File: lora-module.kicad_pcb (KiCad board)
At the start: 4 copper layers, 20.3 x 22.5 mm, 54 parts, among them J101 Conn_Coaxial, J102 Conn_ARM_SWD_TagConnect_TC203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, Q101 PMN48XP, U201 STM32WLE5CCUx, U301 BALFHB-WL-05D3, U302 BGS12SN6E6327XTSA1, U401 SST26VF080A

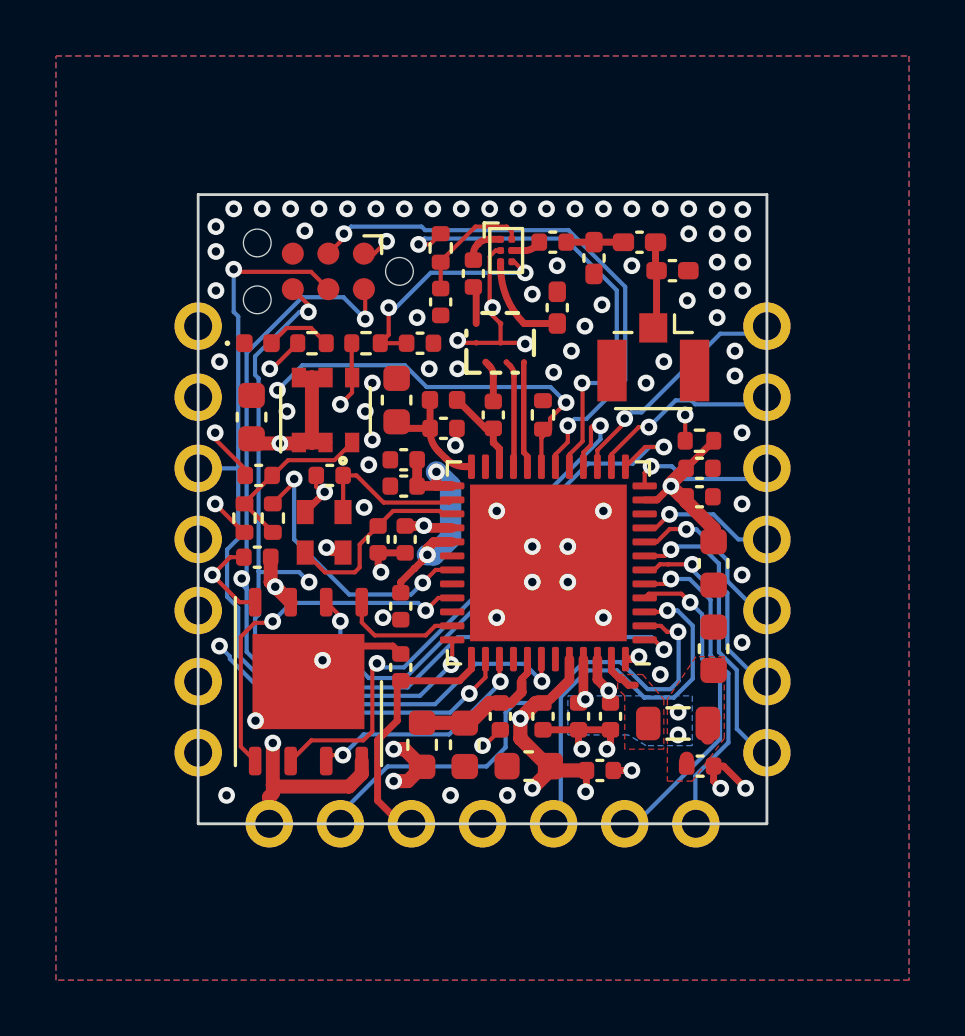
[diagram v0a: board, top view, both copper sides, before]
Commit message: changed XO to TCXO
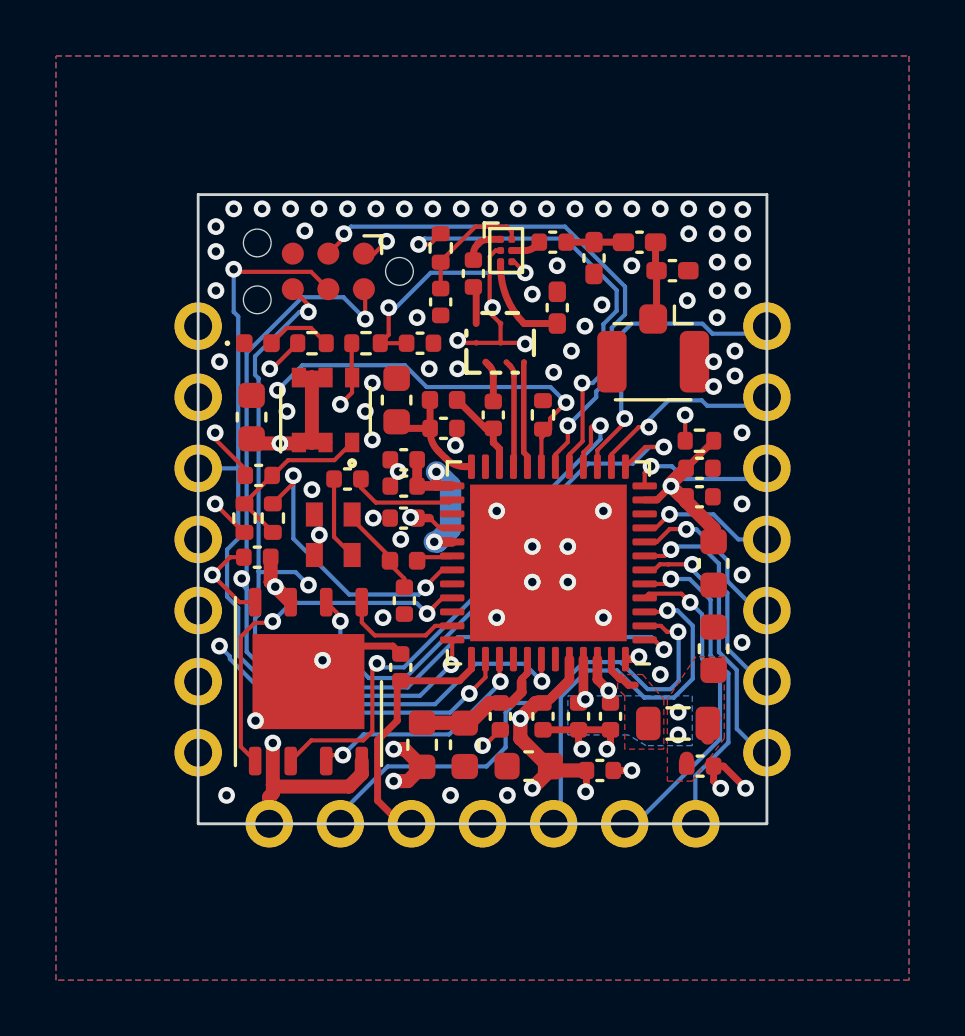
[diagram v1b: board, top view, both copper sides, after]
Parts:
- removed C213: 33p, Capacitor_SMD:C_0402_1005Metric
- removed XTAL201: NX2016SA-32MHZ-EXS00A-CS11336, lora-module:NX2016SA_NDK
- added L203: BLM15HG102SN1D, Inductor_SMD:L_0402_1005Metric, F.Cu at (131.8, 101.9)
- added X201: ECS-TXO-20CSMV4, lora-module:NX2016SA_NDK, F.Cu at (129.3, 100.9)
- C201: value 6.8p -> 33p
- C202: value 6.8 -> 100n
- C217: value 33p -> 100n
- R301, R302: value 100 -> 100R
- moved C202 5.21 mm to (131.8, 103.3), turned to 90 degrees
- moved C201 2.42 mm to (129.8, 98.9), turned to 0 degrees
- moved C209 0.76 mm to (131.8, 100.3), turned to 180 degrees
- moved J101 0.32 mm to (140.7, 94.3)
- moved G*** 0.10 mm to (136.9, 104.0)
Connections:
- C201 pad 1: Net-(U201-OSC_OUT) -> Net-(X201-OUT)
- C201 pad 2: GND -> Net-(U201-OSC_IN)
- C202 pad 2: Net-(U201-OSC_IN) -> Net-(X201-Vcc)
- U201 pad 27: Net-(U201-OSC_OUT) -> unconnected-(U201-OSC_OUT-Pad27)
- U201 pad 30: unconnected-(U201-PB0-Pad30) -> /STM32WL/VDD_TCXO
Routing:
- net Net-(U201-OSC_OUT): track 6.98 -> 0.00 mm
- net GND: track 28.8 -> 24.8 mm
- net Net-(X201-Vcc): track 0.00 -> 3.34 mm
- net /STM32WL/VDDPA: track 20.2 -> 17.2 mm
- net Net-(X201-OUT): track 0.00 -> 2.98 mm
- net /IO1: track 8.92 -> 11.2 mm
- net Net-(U201-OSC_IN): track 5.65 -> 3.83 mm
- net /STM32WL/VDD_TCXO: track 0.00 -> 1.37 mm

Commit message: small tweaks
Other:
- board text added: "03.24"
- board text added: "LoRa 865-923 module v0.2"
- board text removed: "10.23"
- board text removed: "LoRa 865-923 module v0.1"
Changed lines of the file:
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@@
     (effects (font (size 1.2 1.2) (thickness 0.2)) (justify right mirror))
   )
-  (gr_text "LoRa 865-923\n module v0.1" (at 133.096 102.87 270) (layer "B.SilkS")
+  (gr_text "LoRa 865-923\n module v0.2" (at 133.096 102.87 270) (layer "B.SilkS")
     (effects (font (size 1.2 1.2) (thickness 0.25) bold) (justify left bottom mirror))
   )
@@
     (effects (font (size 1.2 1.2) (thickness 0.2)) (justify left mirror))
   )
-  (gr_text "10.23" (at 130.556 97.536 270) (layer "B.SilkS")
+  (gr_text "03.24" (at 130.556 97.536 270) (layer "B.SilkS")
     (effects (font (size 1.2 1.2) (thickness 0.25) bold) (justify left bottom mirror))
   )

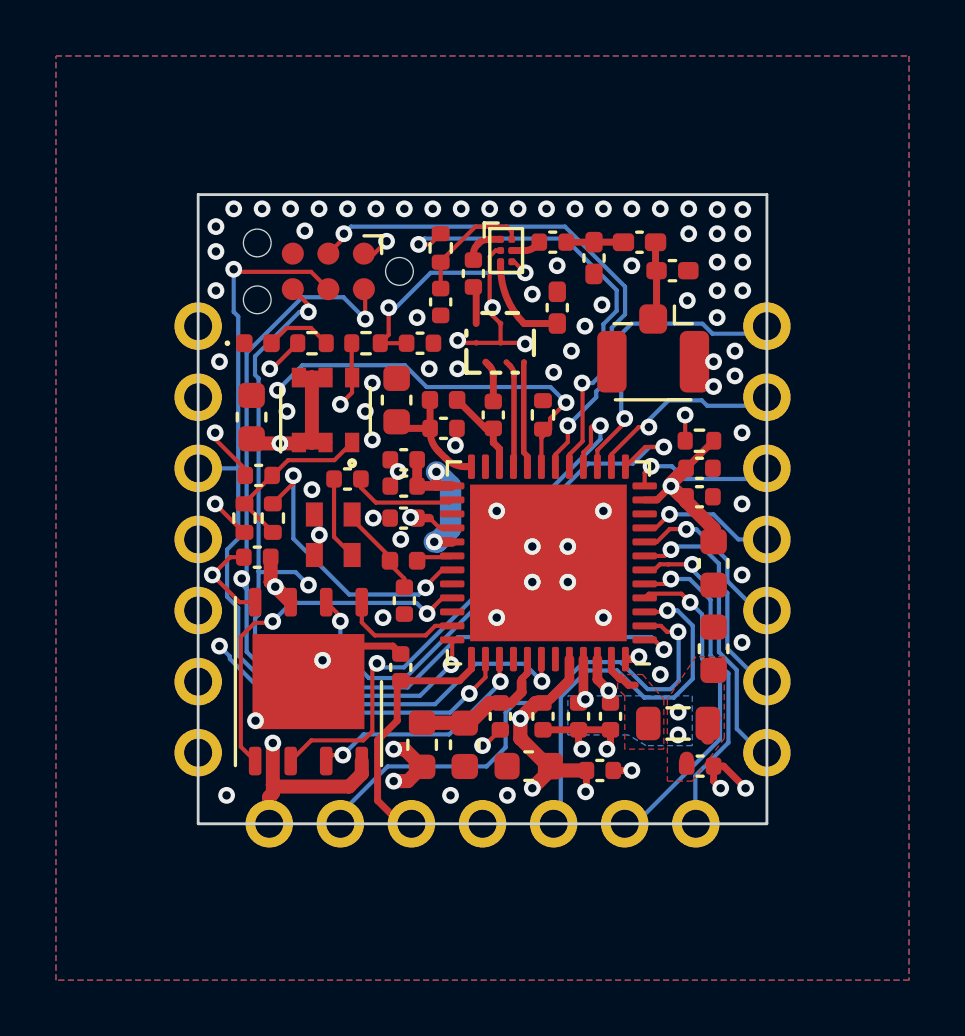
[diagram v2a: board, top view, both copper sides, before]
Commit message: module pinout change
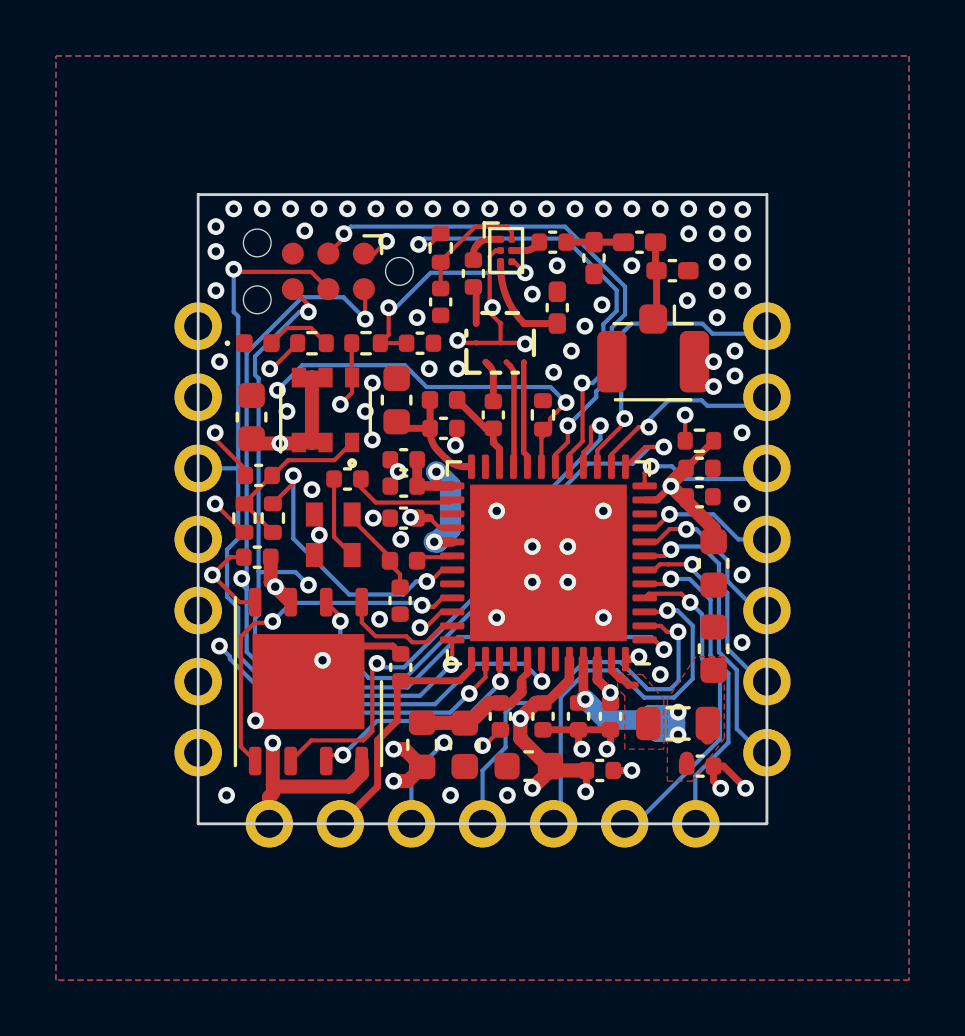
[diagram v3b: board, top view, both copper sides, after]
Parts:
- moved C202 0.15 mm to (131.7, 103.3)
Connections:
- J106 pad 11: GND -> /IO11
- J106 pad 12: /VBAT -> /IO12
- J106 pad 13: /IO11 -> /VBAT
- U201 pad 34: unconnected-(U201-PA11-Pad34) -> /IO12
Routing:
- net /IO12: track 0.00 -> 9.89 mm, vias 0 -> 2
- net /STM32WL/VDDPA: track 17.2 -> 24.6 mm
- net /IO11: track 19.0 -> 14.8 mm
- removed copper zone on B.Cu, net /STM32WL/VDDPA
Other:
- board text added: "12"
- board text added: "VBAT"
- board text removed: "BATT"

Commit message: bom update and other tweaks
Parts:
- removed C201: 33p, Capacitor_SMD:C_0402_1005Metric
- added C1: 39p, Capacitor_SMD:C_0402_1005Metric, F.Cu at (129.8, 98.8)
- J101: value Conn_Coaxial -> U.FL-R-SMT-1(01)
- L202: value 15u -> 15uH
- Q101: value PMN48XP -> PMN48XP,115
- U201: value STM32WLE5CCUx -> STM32WLE5CCU6
- X201: value ECS-TXO-20CSMV4 -> ECS-TXO-20CSMV4-320-AY-TR
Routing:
- net VDD: track 25.7 -> 28.6 mm, vias 11 -> 14
- net GND: vias 88 -> 89
